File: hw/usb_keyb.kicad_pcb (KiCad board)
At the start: 2 copper layers, 99.1 x 48.3 mm, 126 parts, among them J10 SPI, J14 RJ45-TRANSFO, J2 Micro_SD_Card, J3 USB_1, J4 ZX-BUS, J5 MX_ROW, J6 MX_COL, J7 I2C, J8 UART, J9 PROG, SW1 RESET, U1 LM3671MF, U2 STM32F407VETx, U3 STMPS2141STR, U4 STMPS2141STR, U5 DP83848C, Y1 8MHz, Y2 50MHz

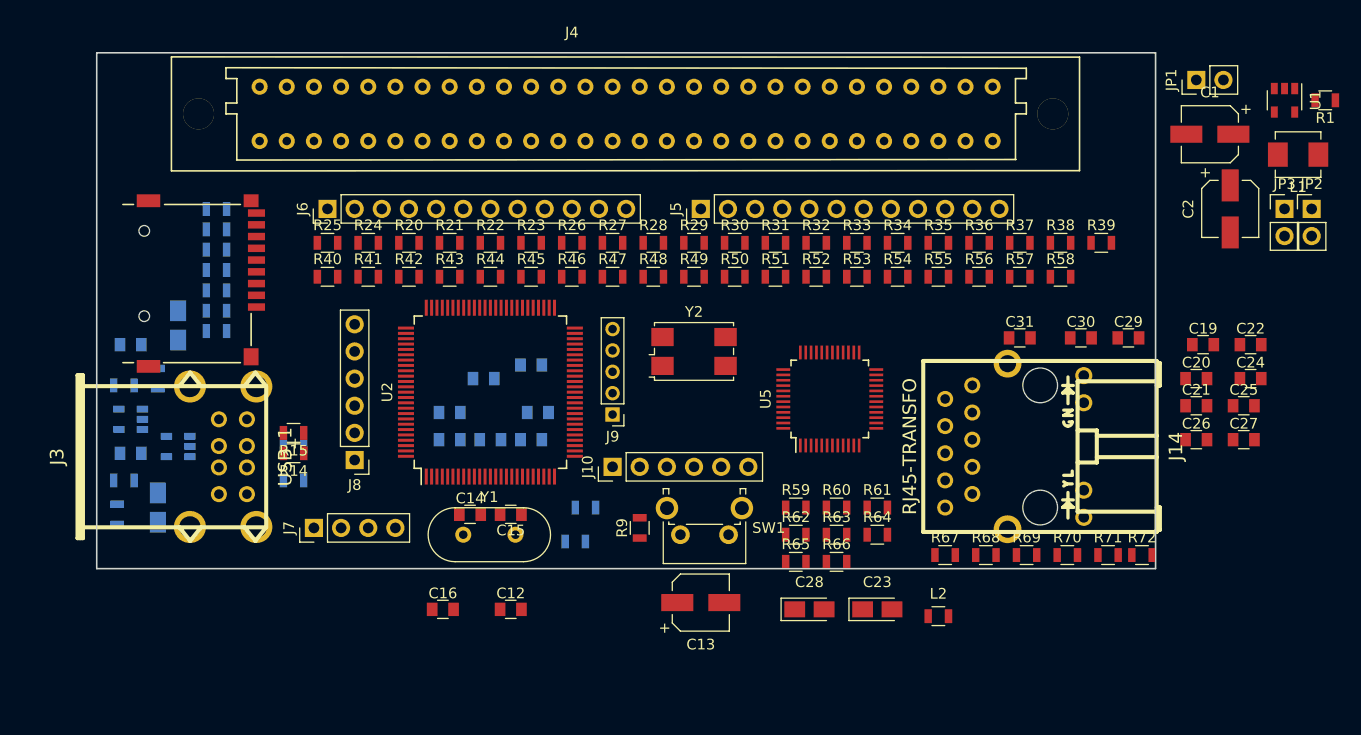
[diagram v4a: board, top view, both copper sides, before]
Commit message: Обновлены плата и схема устройства
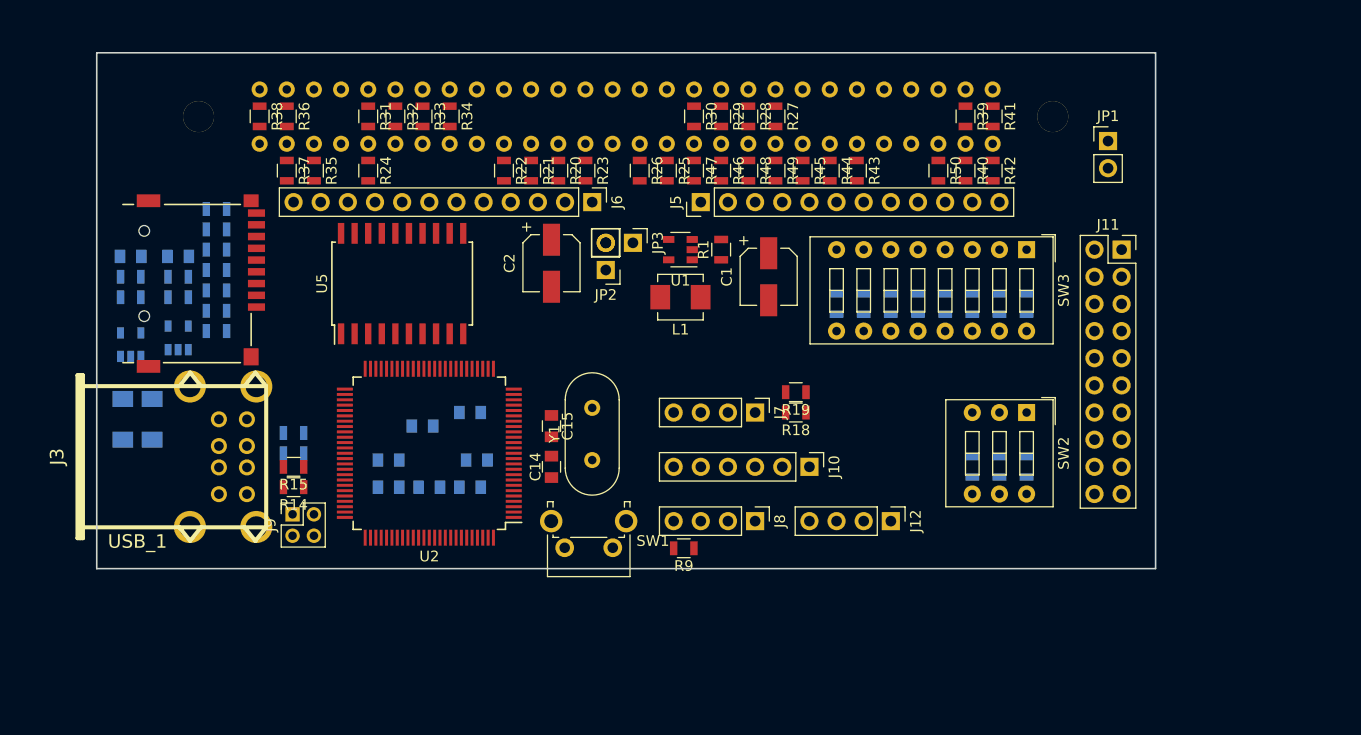
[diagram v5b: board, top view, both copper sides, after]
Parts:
- removed C12, C16, C19, C20, C21, C22, C24, C25, C26, C27, C29, C30, C31: 100n, Capacitors_SMD:C_0805
- removed C13: 100uF, Capacitors_SMD:CP_Elec_5x5.7
- removed C23, C28: 10u, Capacitors_Tantalum_SMD:CP_Tantalum_Case-A_EIA-3216-18_Reflow
- removed J14: RJ45-TRANSFO, Projects:rj45_wurth-7499211122a
- removed L2: 2.2µH, Inductors_SMD:L_0805
- removed R62, R63: 2k, Resistors_SMD:R_0805
- removed R64: 4k7, Resistors_SMD:R_0805
- removed R65: 150, Resistors_SMD:R_0805
- removed R66: 18, Resistors_SMD:R_0805
- removed R67, R68, R69, R70: 51, Resistors_SMD:R_0805
- removed R71, R72: 330, Resistors_SMD:R_0805
- removed Y2: 50MHz, Crystals:Crystal_SMD_7050-4pin_7.0x5.0mm
- added J11: RMII, Socket_Strips:Socket_Strip_Straight_2x10_Pitch2.54mm, F.Cu at (192.4, 78.7)
- added J12: PS2, Socket_Strips:Socket_Strip_Straight_1x04_Pitch2.54mm, F.Cu at (170.8, 104.1)
- added SW2: OUTPUT, Buttons_Switches_THT:SW_DIP_x3_W7.62mm_Slide, F.Cu at (183.5, 94.0)
- added SW3: MATRIX, Buttons_Switches_THT:SW_DIP_x8_W7.62mm_Slide, F.Cu at (183.5, 78.7)
- J4, R51, R52, R53, R54, R55, R56, R57, R58, R61: moved to B.Cu
- J8: footprint Socket_Strips:Socket_Strip_Straight_1x06_Pitch2.54mm -> Socket_Strips:Socket_Strip_Straight_1x04_Pitch2.54mm
- J9: footprint Socket_Strips:Socket_Strip_Straight_1x05_Pitch2.00mm -> Socket_Strips:Socket_Strip_Straight_2x02_Pitch2.00mm
- R18, R19: moved to F.Cu
- R59, R60: value 2k -> 10k; moved to B.Cu
- U5: value DP83848C -> 74LS245; footprint Housings_QFP:LQFP-48_7x7mm_Pitch0.5mm -> Housings_SOIC:SOIC-20W_7.5x12.8mm_Pitch1.27mm
- moved R38 75.9 mm to (111.8, 66.3), turned to 270 degrees
- moved R37 68.9 mm to (114.3, 71.3), turned to 270 degrees
- moved JP2 66.3 mm to (144.1, 80.6), turned to 180 degrees
- moved R36 65.8 mm to (114.3, 66.3), turned to 270 degrees
- moved C2 63.7 mm to (139.1, 80.0)
- moved JP3 61.0 mm to (146.7, 78.1), turned to 270 degrees
- moved R40 60.5 mm to (177.8, 71.3), turned to 270 degrees
- moved R41 60.3 mm to (180.3, 66.3), turned to 270 degrees
- moved L1 59.3 mm to (151.1, 83.2)
- moved R35 58.8 mm to (116.8, 71.3), turned to 270 degrees
- moved R1 58.2 mm to (154.9, 78.7), turned to 90 degrees
- moved U1 58.2 mm to (151.1, 78.7), turned to 180 degrees
- moved R42 55.5 mm to (180.3, 71.3), turned to 270 degrees
- moved R34 43.5 mm to (129.5, 66.3), turned to 270 degrees
- moved C1 43.4 mm to (159.4, 81.3), turned to 270 degrees
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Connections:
- net Net-(U2-Pad81) renamed LED_1
- net Net-(U2-Pad82) renamed LED_2
- net Net-(U2-Pad85) renamed LED_3
- net RX renamed Net-(U2-Pad69)
- J4 pad 3b: +5 -> +5V
- J5 pad 10: MR9 -> ZA1
- J5 pad 11: MR10 -> ZA2
- J5 pad 12: MR11 -> ZA3
- J5 pad 9: MR8 -> ZA0
- J6 pad 1: ZD0 -> D0
- J6 pad 10: MC9 -> ZA5
- J6 pad 11: MC10 -> ZA6
- J6 pad 12: MC11 -> ZA7
- J6 pad 2: ZD1 -> D1
- J6 pad 3: ZD2 -> D2
- J6 pad 4: ZD3 -> D3
- J6 pad 5: ZD4 -> D4
- J6 pad 6: ZD5 -> D5
- J6 pad 7: ZD6 -> D6
- J6 pad 8: ZD7 -> D7
- J6 pad 9: MC8 -> ZA4
- J8 pad 1: UART_CTS -> UART_TX
- J8 pad 2: UART_RTS -> UART_RX
- J8 pad 3: UART_TX -> +3V3
- J8 pad 4: UART_RX -> GND
- J9 pad 2: SWDIO -> SWCLK
- J9 pad 3: SWCLK -> SWDIO
- J9 pad 4: +3V3 -> GND
- R24 pad 1: +5V -> +3V3
- R24 pad 2: ZA8 -> ZM1n
- R25 pad 1: +5V -> +3V3
- R25 pad 2: ZA9 -> ZINTn
- R26 pad 1: +5V -> +3V3
- R26 pad 2: ZA10 -> ZNMIn
- R27 pad 1: +5V -> +3V3
- R27 pad 2: ZA11 -> ZA0
- R28 pad 1: +5V -> +3V3
- R28 pad 2: ZA12 -> ZA1
- R29 pad 1: +5V -> +3V3
- R29 pad 2: ZA13 -> ZA2
- R30 pad 1: +5V -> +3V3
- R30 pad 2: ZA14 -> ZA3
- R31 pad 1: +5V -> +3V3
- R31 pad 2: ZA15 -> ZA4
- R32 pad 1: +5V -> +3V3
- R32 pad 2: MR8 -> ZA5
- R33 pad 1: +5V -> +3V3
- R33 pad 2: MR9 -> ZA6
- R34 pad 1: +5V -> +3V3
- R34 pad 2: MR10 -> ZA7
- R35 pad 2: MR11 -> ZA8
- R36 pad 2: ZD0 -> ZA9
- R37 pad 2: ZD1 -> ZA10
- R38 pad 2: ZD2 -> ZA11
- R39 pad 2: ZD3 -> ZA12
- R40 pad 2: ZD4 -> ZA13
- R41 pad 2: ZD5 -> ZA14
- R42 pad 2: ZD6 -> ZA15
- R43 pad 2: ZD7 -> ZD0
- R44 pad 2: MC8 -> ZD1
- R45 pad 2: MC9 -> ZD2
- R46 pad 2: MC10 -> ZD3
- R47 pad 2: MC11 -> ZD4
- R48 pad 1: +3V3 -> +5V
- R48 pad 2: ZM1n -> ZD5
- R49 pad 1: +3V3 -> +5V
- R49 pad 2: ZINTn -> ZD6
- R50 pad 1: +3V3 -> +5V
- R50 pad 2: ZNMIn -> ZD7
- R51 pad 2: ZA0 -> OUT0
- R52 pad 2: ZA1 -> OUT1
- R53 pad 2: ZA2 -> OUT2
- R54 pad 2: ZA3 -> MTX0
- R55 pad 2: ZA4 -> MTX1
- R56 pad 2: ZA5 -> MTX2
- R57 pad 2: ZA6 -> MTX3
- R58 pad 2: ZA7 -> MTX4
- R59 pad 2: Net-(R59-Pad2) -> MTX5
- R60 pad 2: CRS -> MTX6
- R61 pad 2: Net-(R61-Pad2) -> MTX7
- U2 pad 1: Net-(U2-Pad1) -> ZA2
- U2 pad 15: Net-(U2-Pad15) -> MTX4
- U2 pad 17: Net-(U2-Pad17) -> PS2_CLK
- U2 pad 18: Net-(U2-Pad18) -> PS2_DAT
- U2 pad 2: Net-(U2-Pad2) -> ZA3
- U2 pad 23: Net-(U2-Pad23) -> ZM1n
- U2 pad 26: Net-(U2-Pad26) -> MTX0
- U2 pad 29: PA4 -> MTX1
- U2 pad 3: Net-(U2-Pad3) -> ZA4
- U2 pad 30: Net-(U2-Pad30) -> MTX2
- U2 pad 31: Net-(U2-Pad31) -> MTX3
- U2 pad 35: Net-(U2-Pad35) -> ZIORQn
- U2 pad 36: Net-(U2-Pad36) -> ZRDn
- U2 pad 37: Net-(U2-Pad37) -> ZWRn
- U2 pad 38: Net-(U2-Pad38) -> ZA7
- U2 pad 39: Net-(U2-Pad39) -> D0
- U2 pad 4: Net-(U2-Pad4) -> ZA5
- U2 pad 40: Net-(U2-Pad40) -> D1
- U2 pad 41: Net-(U2-Pad41) -> D2
- U2 pad 42: Net-(U2-Pad42) -> D3
- U2 pad 43: Net-(U2-Pad43) -> D4
- U2 pad 44: Net-(U2-Pad44) -> D5
- U2 pad 45: Net-(U2-Pad45) -> D6
- U2 pad 46: Net-(U2-Pad46) -> D7
- U2 pad 47: Net-(U2-Pad47) -> ZNMIn
- U2 pad 5: Net-(U2-Pad5) -> ZA6
- U2 pad 55: Net-(U2-Pad55) -> ZA8
- U2 pad 56: Net-(U2-Pad56) -> ZA9
- U2 pad 57: Net-(U2-Pad57) -> ZA10
- U2 pad 58: Net-(U2-Pad58) -> ZA11
- U2 pad 59: Net-(U2-Pad59) -> ZA12
- U2 pad 60: Net-(U2-Pad60) -> ZA13
- U2 pad 61: Net-(U2-Pad61) -> ZA14
- U2 pad 62: Net-(U2-Pad62) -> ZA15
- U2 pad 63: HS_PWR -> UART_TX
- U2 pad 64: CD -> UART_RX
- U2 pad 68: TX -> HS_PWR
- U2 pad 7: Net-(U2-Pad7) -> MTX5
- U2 pad 8: Net-(U2-Pad8) -> MTX6
- U2 pad 84: Net-(U2-Pad84) -> CD
- U2 pad 86: Net-(U2-Pad86) -> OUT0
- U2 pad 87: Net-(U2-Pad87) -> OUT1
- U2 pad 88: Net-(U2-Pad88) -> OUT2
- U2 pad 89: Net-(U2-Pad89) -> SPI_SCK
- U2 pad 9: Net-(U2-Pad9) -> MTX7
- U2 pad 90: Net-(U2-Pad90) -> SPI_MISO
- U2 pad 91: Net-(U2-Pad91) -> SPI_MOSI
- U2 pad 92: Net-(U2-Pad92) -> SCL
- U2 pad 93: Net-(U2-Pad93) -> SDA
- U2 pad 95: Net-(U2-Pad95) -> ZMREQn
- U2 pad 96: Net-(U2-Pad96) -> ZINTn
- U2 pad 97: Net-(U2-Pad97) -> ZA0
- U2 pad 98: Net-(U2-Pad98) -> ZA1
- U5 pad 1: Net-(U5-Pad1) -> PS2_DAT
- U5 pad 10: (no net) -> GND
- U5 pad 11: (no net) -> ZD0
- U5 pad 12: (no net) -> ZD1
- U5 pad 13: RD- -> ZD2
- U5 pad 14: RD+ -> ZD3
- U5 pad 15: GND -> ZD4
- U5 pad 16: TD- -> ZD5
- U5 pad 17: TD+ -> ZD6
- U5 pad 18: PFB -> ZD7
- U5 pad 19: GND -> PS2_CLK
- U5 pad 2: Net-(U5-Pad2) -> D7
- U5 pad 20: Net-(R62-Pad1) -> VCC
- U5 pad 3: TXD0 -> D6
- U5 pad 4: TXD1 -> D5
- U5 pad 5: Net-(U5-Pad5) -> D4
- U5 pad 6: Net-(U5-Pad6) -> D3
- U5 pad 7: Net-(U5-Pad7) -> D2
- U5 pad 8: (no net) -> D1
- U5 pad 9: (no net) -> D0

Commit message: Обновлена плата
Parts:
- removed C10, C11: 100n, Capacitors_SMD:C_0805
- U5: moved to B.Cu
- moved C1 28.7 mm to (186.7, 72.4)
- moved J5 26.0 mm to (179.1, 74.3), turned to 270 degrees
- moved R61 21.8 mm to (183.0, 97.1), turned to 0 degrees
- moved R4 20.8 mm to (107.7, 101.5), turned to 0 degrees
- moved R5 20.8 mm to (107.7, 99.6), turned to 0 degrees
- moved R6 20.8 mm to (107.7, 97.7), turned to 0 degrees
- moved R7 20.8 mm to (107.7, 95.8), turned to 0 degrees
- moved C2 19.7 mm to (158.8, 80.6)
- moved JP2 19.7 mm to (163.8, 80.6)
- moved JP3 19.7 mm to (166.4, 78.1)
- moved L1 19.7 mm to (170.8, 83.2)
- moved R1 19.7 mm to (174.6, 78.7)
- moved U1 19.7 mm to (170.8, 78.7)
- moved R60 18.3 mm to (183.0, 94.6), turned to 0 degrees
- moved C18 17.9 mm to (98.3, 78.7)
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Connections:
- net FS_D+ renamed FS_P
- net FS_D- renamed FS_N
- net HS_D+ renamed HS_P
- net HS_D- renamed HS_N
- net Net-(J3-Pad2) renamed /F_N
- net Net-(J3-Pad3) renamed /F_P
- net Net-(J3-Pad6) renamed /H_N
- net Net-(J3-Pad7) renamed /H_P
- J2 pad 1: D2 -> SD2
- J2 pad 2: D3 -> SD3
- J2 pad 7: D0 -> SD0
- J2 pad 8: D1 -> SD1
- U2 pad 65: D0 -> SD0
- U2 pad 66: D1 -> SD1
- U2 pad 78: D2 -> SD2
- U2 pad 79: D3 -> SD3
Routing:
- net CMD: track 0.00 -> 16.5 mm, vias 0 -> 2
- net CK: track 0.00 -> 16.5 mm, vias 0 -> 2
- net SWDIO: track 0.00 -> 15.2 mm, vias 0 -> 2
- net SD0: track 0.00 -> 14.7 mm
- net SD1: track 0.00 -> 13.8 mm
- net SD3: track 0.00 -> 13.1 mm, vias 0 -> 2
- net SD2: track 0.00 -> 12.2 mm, vias 0 -> 2
- net SWCLK: track 0.00 -> 11.7 mm
- net FS_N: track 0.00 -> 9.93 mm
- net FS_P: track 0.00 -> 9.29 mm
- net /F_N: track 0.00 -> 8.58 mm
- net /F_P: track 0.00 -> 7.69 mm
- net HS_N: track 0.00 -> 6.14 mm, vias 0 -> 1
- net HS_P: track 0.00 -> 5.69 mm, vias 0 -> 1
- net /H_P: track 0.00 -> 4.60 mm
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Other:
- net class Default: clearance 0.2 -> 0.175; trace_width 0.25 -> 0.175
- rule trace_clearance: 0.2 -> 0.175
- rule trace_min: 0.2 -> 0.175
- rule via_min_drill: 0.3 -> 0.2

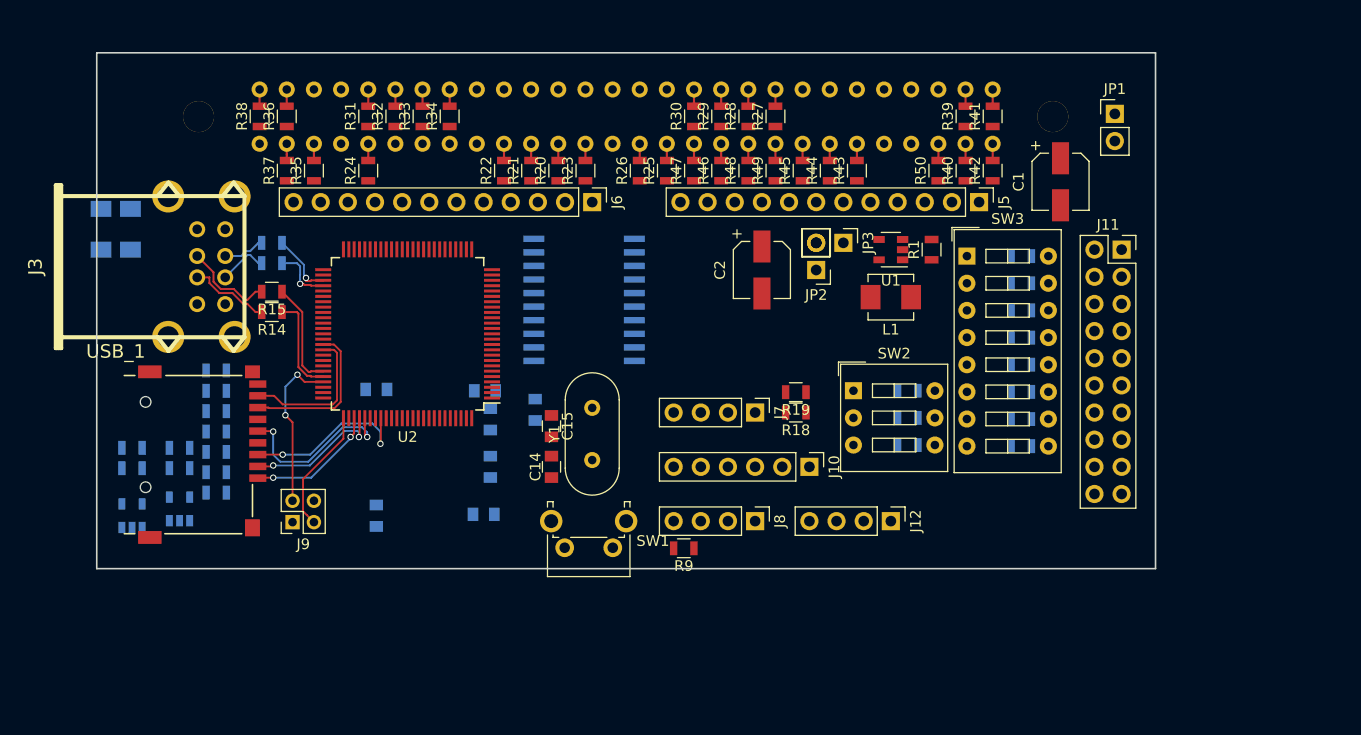
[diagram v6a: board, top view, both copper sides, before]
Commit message: Обновлены назначение выводов и плата
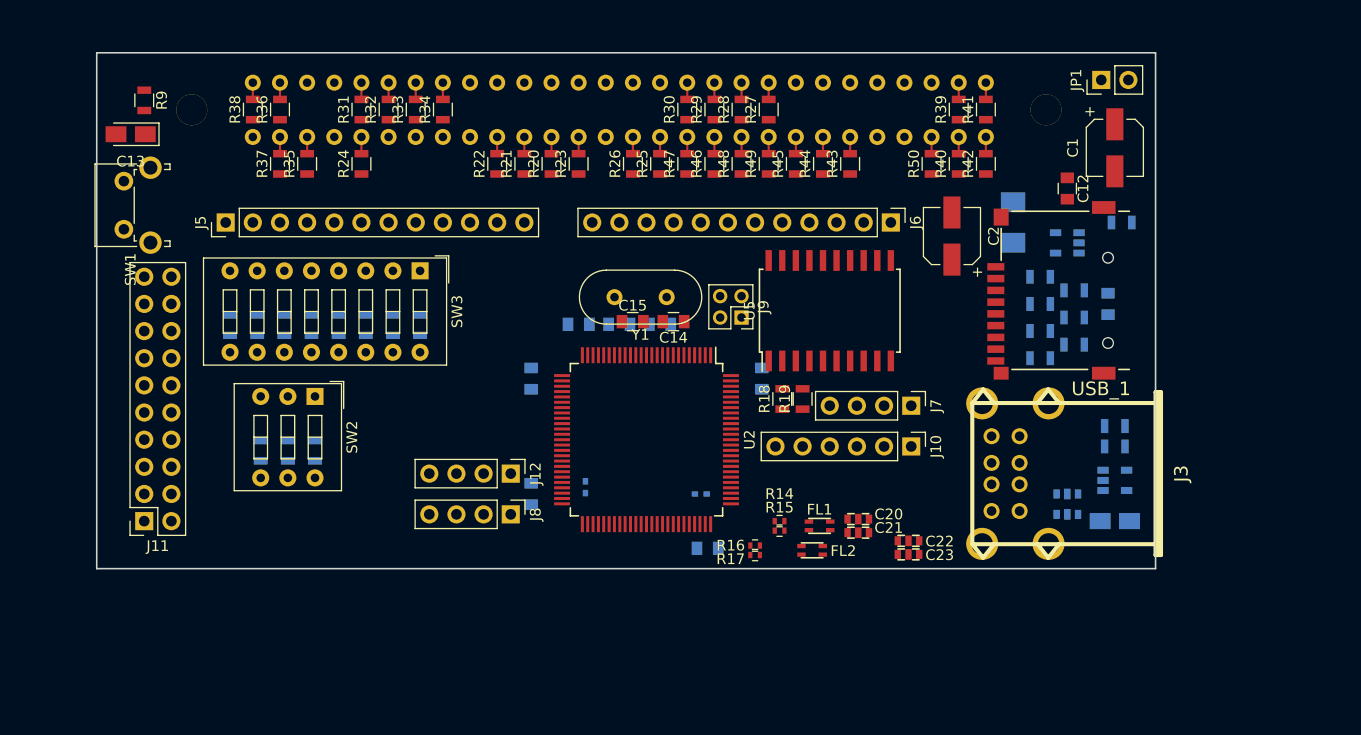
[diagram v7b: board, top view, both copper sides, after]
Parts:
- removed JP2: 5Vin, Pin_Headers:Pin_Header_Straight_1x02_Pitch2.54mm
- removed JP3: 3Vin, Pin_Headers:Pin_Header_Straight_1x02_Pitch2.54mm
- removed R11: 0, Resistors_SMD:R_0805
- removed R13: 10k, Resistors_SMD:R_0805
- removed U4: STMPS2141STR, TO_SOT_Packages_SMD:SOT-23-5
- added C12: 100n, Capacitors_SMD:C_0805, F.Cu at (187.3, 73.0)
- added C13: 10uF, Capacitors_Tantalum_SMD:CP_Tantalum_Case-A_EIA-3216-18_Reflow, F.Cu at (99.7, 67.9)
- added C16: 100n, Capacitors_SMD:C_0805, B.Cu at (191.1, 83.8)
- added C19: 2,2u, Capacitors_SMD:C_0402, B.Cu at (142.2, 101.0)
- added C20: NFM21PC104R1E3D, Projects:NFM21P, F.Cu at (167.8, 103.9)
- added C21: NFM21PC104R1E3D, Projects:NFM21P, F.Cu at (167.8, 105.2)
- added C22: NFM21PC104R1E3D, Projects:NFM21P, F.Cu at (172.5, 106.0)
- added C23: NFM21PC104R1E3D, Projects:NFM21P, F.Cu at (172.5, 107.3)
- added C24: NFM21PC104R1E3D, Projects:NFM21P, B.Cu at (187.3, 101.6)
- added C25: NFM21PC104R1E3D, Projects:NFM21P, B.Cu at (187.3, 103.5)
- added FL1: DLW21SN371SQ2, Projects:DLW21S, F.Cu at (164.1, 104.6)
- added FL2: DLW21SN371SQ2, Projects:DLW21S, F.Cu at (163.4, 106.9)
- C18: value 4,7uF -> 2,2u; footprint Capacitors_Tantalum_SMD:CP_Tantalum_Case-A_EIA-3216-18_Reflow -> Capacitors_SMD:C_0402
- L1, R1, U1: moved to B.Cu
- R14, R15: footprint Resistors_SMD:R_0805 -> Resistors_SMD:R_0402
- R16, R17: footprint Resistors_SMD:R_0805 -> Resistors_SMD:R_0402; moved to F.Cu
- U3: value STMPS2141STR -> STMPS2161STR
- U5: moved to F.Cu
- moved C17 97.9 mm to (191.8, 104.1), turned to 0 degrees
- moved J11 94.9 mm to (101.0, 104.1), turned to 180 degrees
- moved J2 91.3 mm to (191.1, 82.5), turned to 90 degrees
- moved J3 88.0 mm to (187.3, 99.7), turned to 90 degrees
- moved U3 87.5 mm to (191.8, 100.3), turned to 0 degrees
- moved R10 87.5 mm to (191.8, 95.2), turned to 0 degrees
- moved R12 87.5 mm to (191.8, 97.2), turned to 0 degrees
- moved R5 82.0 mm to (188.0, 82.5), turned to 180 degrees
- moved R7 81.0 mm to (188.0, 85.1), turned to 180 degrees
- moved R3 80.4 mm to (188.0, 87.6), turned to 180 degrees
- moved R4 79.7 mm to (184.8, 81.3), turned to 180 degrees
- moved R6 78.3 mm to (184.8, 83.8), turned to 180 degrees
- moved R2 77.5 mm to (184.8, 86.4), turned to 180 degrees
- moved R8 77.1 mm to (184.8, 88.9), turned to 180 degrees
- moved R61 74.9 mm to (109.0, 85.8), turned to 270 degrees
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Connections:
- C1 pad 1: Net-(C1-Pad1) -> +5V
- C18 pad 1: Net-(C18-Pad1) -> VC2
- J3 pad 1: Net-(C17-Pad1) -> Net-(C24-Pad3)
- J3 pad 2: /F_N -> F2_N
- J3 pad 3: /F_P -> F2_P
- J3 pad 5: Net-(C18-Pad1) -> Net-(C25-Pad3)
- J3 pad 6: /H_N -> H2_N
- J3 pad 7: /H_P -> H2_P
- L1 pad 2: Net-(JP2-Pad1) -> +3V3
- R1 pad 1: Net-(C1-Pad1) -> +5V
- R10 pad 1: FS_PWR -> USB_PWR
- R14 pad 2: /F_P -> /F1_P
- R15 pad 2: /F_N -> /F1_N
- R16 pad 2: /H_P -> /H1_P
- R17 pad 2: /H_N -> /H1_N
- R2 pad 2: D0 -> SD0
- R3 pad 2: D1 -> SD1
- R4 pad 2: D2 -> SD2
- R5 pad 2: D3 -> SD3
- U1 pad 1: Net-(C1-Pad1) -> +5V
- U1 pad 4: Net-(JP2-Pad1) -> +3V3
- U2 pad 15: MTX4 -> MTX2
- U2 pad 17: PS2_CLK -> MTX3
- U2 pad 18: PS2_DAT -> MTX4
- U2 pad 21: VR+ -> +3V3
- U2 pad 23: ZM1n -> Net-(U2-Pad23)
- U2 pad 30: MTX2 -> PS2_CLK
- U2 pad 31: MTX3 -> PS2_DAT
- U2 pad 35: ZIORQn -> LED_1
- U2 pad 36: ZRDn -> LED_2
- U2 pad 37: ZWRn -> LED_3
- U2 pad 39: D0 -> ZA8
- U2 pad 40: D1 -> ZA9
- U2 pad 41: D2 -> ZA10
- U2 pad 42: D3 -> ZA11
- U2 pad 43: D4 -> ZA12
- U2 pad 44: D5 -> ZA13
- U2 pad 45: D6 -> ZA14
- U2 pad 46: D7 -> ZA15
- U2 pad 47: ZNMIn -> ZM1n
- U2 pad 55: ZA8 -> D0
- U2 pad 56: ZA9 -> D1
- U2 pad 57: ZA10 -> D2
- U2 pad 58: ZA11 -> D3
- U2 pad 59: ZA12 -> D4
- U2 pad 60: ZA13 -> D5
- U2 pad 61: ZA14 -> D6
- U2 pad 62: ZA15 -> D7
- U2 pad 67: FS_PWR -> OUT0
- U2 pad 68: HS_PWR -> OUT1
- U2 pad 69: Net-(U2-Pad69) -> OUT2
- U2 pad 81: LED_1 -> ZINTn
- U2 pad 82: LED_2 -> ZNMIn
- U2 pad 85: LED_3 -> ZIORQn
- U2 pad 86: OUT0 -> ZRDn
- U2 pad 87: OUT1 -> ZWRn
- U2 pad 88: OUT2 -> ZMREQn
- U2 pad 95: ZMREQn -> USB_PWR
- U2 pad 96: ZINTn -> Net-(U2-Pad96)
- U5 pad 20: VCC -> +5V
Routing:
- net CMD: track 16.5 -> 0.00 mm, vias 2 -> 0
- net CK: track 16.5 -> 0.00 mm, vias 2 -> 0
- net SWDIO: track 15.2 -> 0.00 mm, vias 2 -> 0
- net SD0: track 14.7 -> 0.00 mm
- net SD1: track 13.8 -> 0.00 mm
- net SD3: track 13.1 -> 0.00 mm, vias 2 -> 0
- net SD2: track 12.2 -> 0.00 mm, vias 2 -> 0
- net SWCLK: track 11.7 -> 0.00 mm
- net FS_N: track 9.93 -> 0.00 mm
- net FS_P: track 9.29 -> 0.00 mm
- net /F_N: track 8.58 -> 0.00 mm
- net /F_P: track 7.69 -> 0.00 mm
- net HS_N: track 6.14 -> 0.00 mm, vias 1 -> 0
- net HS_P: track 5.69 -> 0.00 mm, vias 1 -> 0
- net /H_P: track 4.60 -> 0.00 mm
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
